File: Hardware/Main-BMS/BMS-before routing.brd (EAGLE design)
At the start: 153.4 x 107.6 mm, 121 parts, among them IC2 TLC6C5912-Q1, J1 SL03THROUGH_HOLE, J2 SL03THROUGH_HOLE, Q1 2N7002PW, Q10 2N7002PW, Q11 2N7002PW, Q12 2N7002PW, Q13 2N7002PW, Q14 2N7002PW, Q15 2N7002PW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

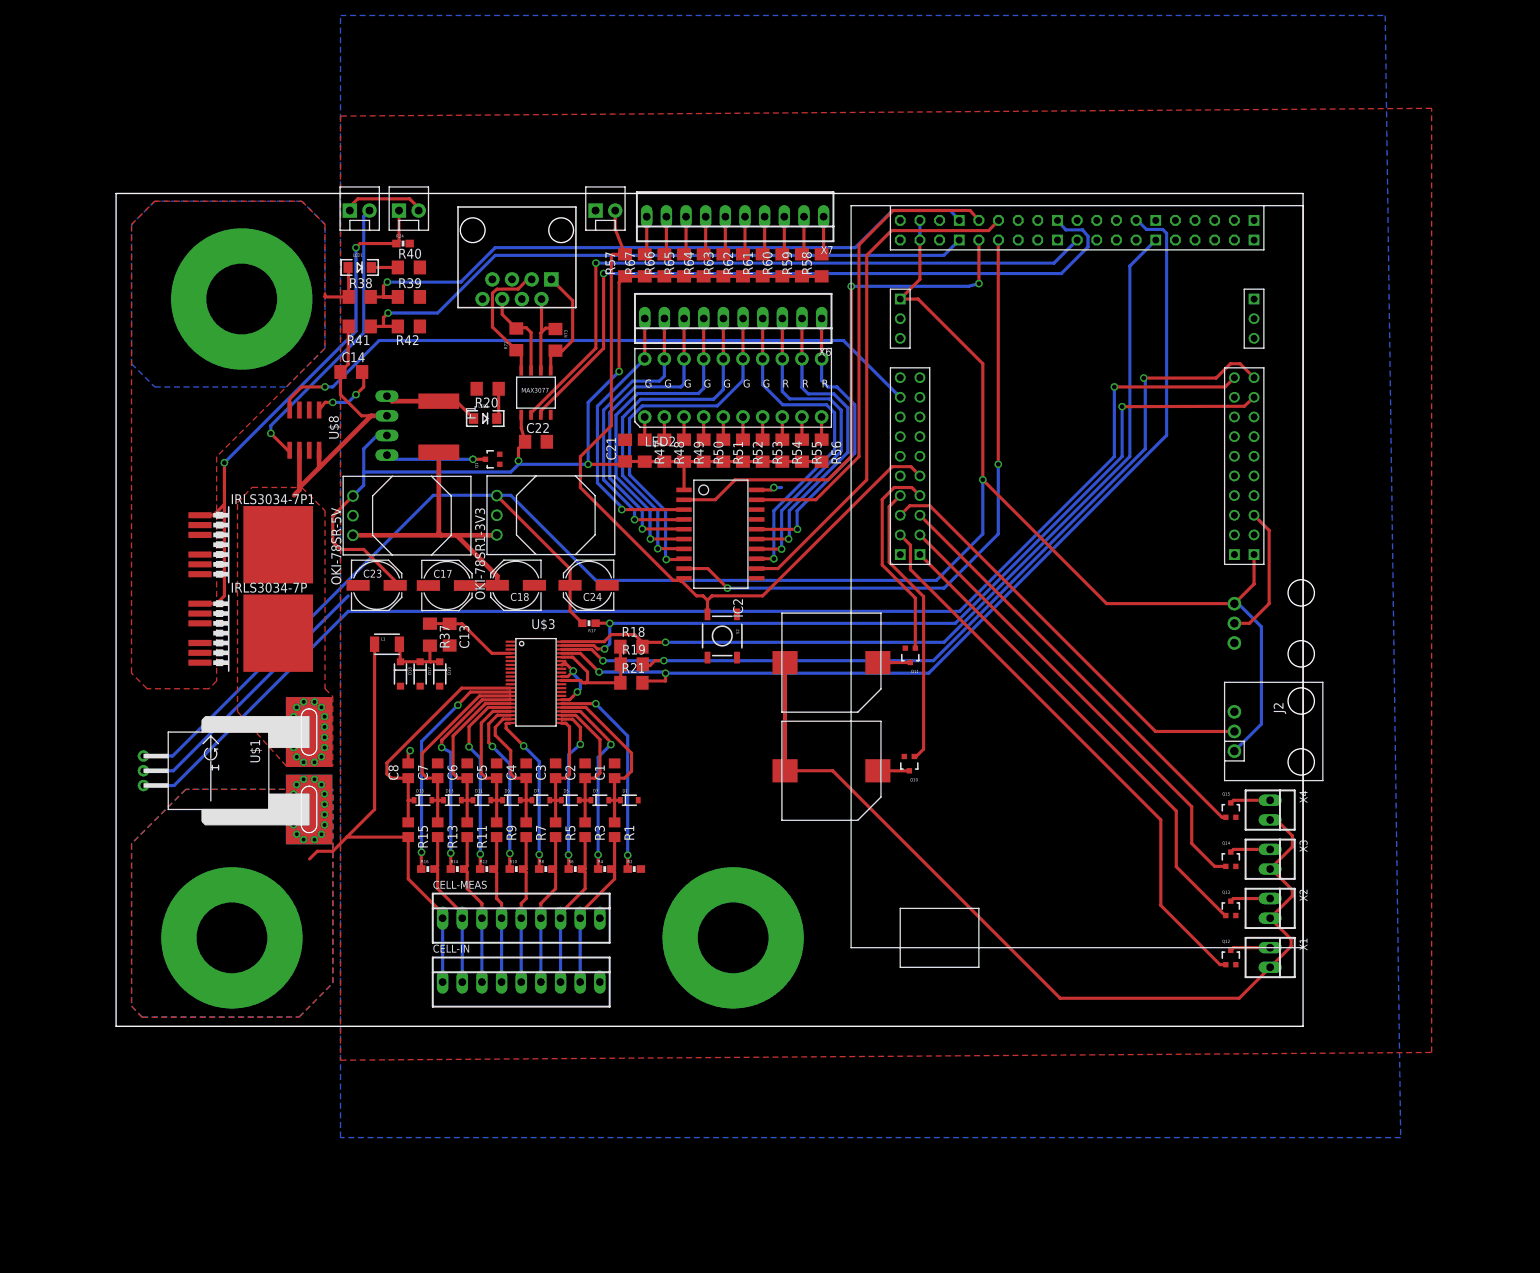
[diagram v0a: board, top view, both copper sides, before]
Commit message: PCB progress
First attempt at PCB design for BMS is mostly done
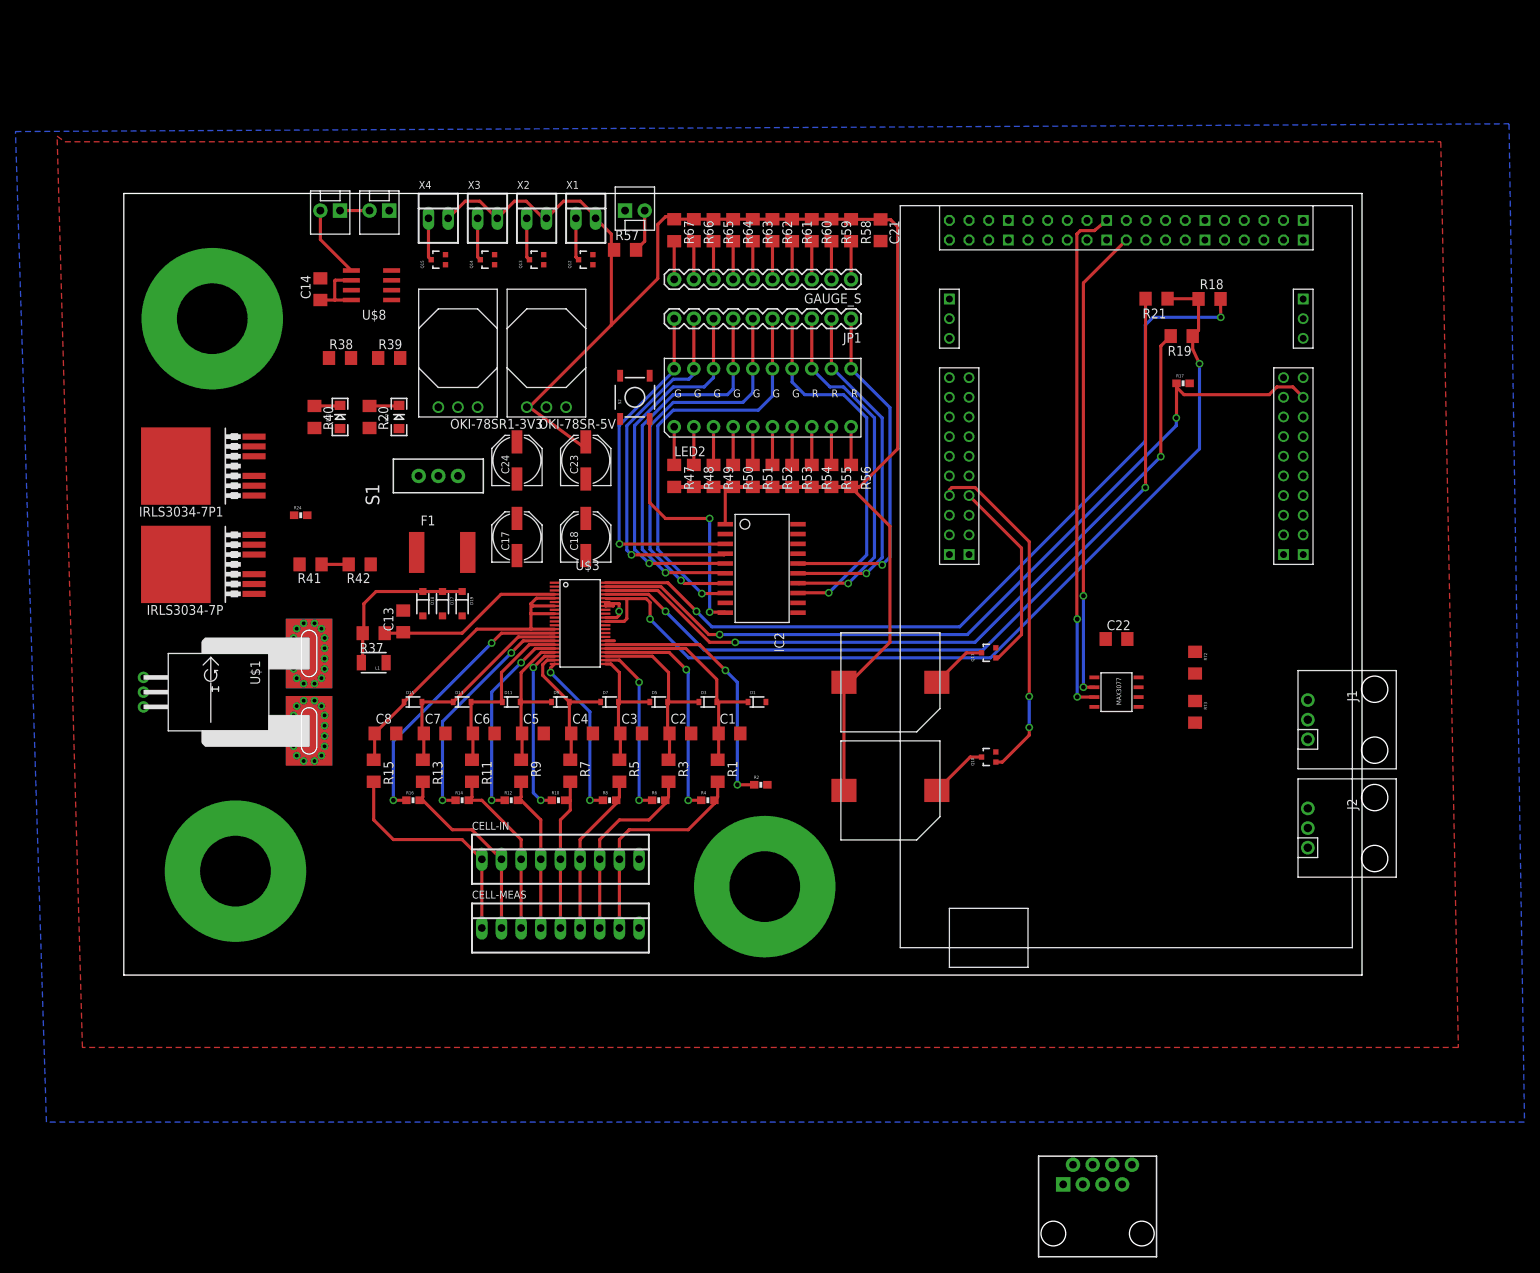
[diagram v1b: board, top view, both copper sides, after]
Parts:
- removed Q1: 2N7002PW, SparkFun-DiscreteSemi:SOT323
- removed X5: 22-23-2041, con-molex:22-23-2041
- removed X6, X7: 22-23-2101, con-molex:22-23-2101
- added GAUGE_S, JP1: M10", SparkFun-Connectors:1X10
- added S1: (no value), SparkFun-Electromechanical:SWITCH-SPDT
- C1, C2, C3, C4, C5, C6, C7, C8: device rcl:C0805 -> rcl:C1206
- R1, R11, R13, R15, R3, R5, R7, R9: device rcl:R0805 -> rcl:R1206
- moved U$14 149.8 mm to (125.8, -34.4), turned to 0 degrees
- moved X4 131.9 mm to (40.6, 96.8), turned to 0 degrees
- moved X3 130.7 mm to (47.0, 96.8), turned to 0 degrees
- moved X1 130.2 mm to (59.7, 96.8), turned to 0 degrees
- moved X2 130.1 mm to (53.3, 96.8), turned to 0 degrees
- moved Q15 124.7 mm to (40.6, 91.4), turned to 90 degrees
- moved Q14 123.4 mm to (47.0, 91.4), turned to 90 degrees
- moved Q12 122.8 mm to (59.7, 91.4), turned to 90 degrees
- moved Q13 122.8 mm to (53.3, 91.4), turned to 90 degrees
- moved R72 97.2 mm to (138.4, 39.4), turned to 270 degrees
- moved R73 95.6 mm to (138.4, 33.0)
- moved R18 87.2 mm to (140.3, 86.4)
- moved U$15 84.4 mm to (128.3, 35.6), turned to 270 degrees
- moved R21 84.1 mm to (133.4, 86.4), turned to 180 degrees
- moved R17 82.8 mm to (136.9, 75.5), turned to 0 degrees
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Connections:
- removed net LOGIC_SWITCH: Q1.1, U$13.3.3
- removed net N$5: Q1.3, X5.1
- new net CHARGER_CTL_B: U$13.7.6
- new net CHARGER_CTL_T: U$13.8.0
- new net CHARGER_I_MEAS: U$13.5.2
- new net V_CHECK_CHARGER_IN: U$13.5.1
- net 5V: no longer X5.2
- net FAN_CTL_1: now also U$13.2.4; no longer U$13.2.5
- net FAN_CTL_2: now also U$13.2.5; no longer U$13.2.7
- net FAN_CTL_4: now also U$13.2.7; no longer U$13.2.4
- net GAUGE_D: now also JP1.7; no longer X6.7
- net GND: now also S1.3; no longer Q1.2
- net N$2: now also S1.2; no longer X5.4
- net N$32: now also JP1.10; no longer X6.10
- net N$41: now also S1.1; no longer X5.3
- net N$43: now also JP1.9; no longer X6.9
- net N$44: now also JP1.8; no longer X6.8
- net N$46: now also JP1.6; no longer X6.6
- net N$47: now also JP1.5; no longer X6.5
- net N$48: now also JP1.4; no longer X6.4
- net N$49: now also JP1.3; no longer X6.3
- net N$50: now also JP1.2; no longer X6.2
- net N$51: now also JP1.1; no longer X6.1
- net N$75: now also GAUGE_S.1; no longer X7.1
- net N$76: now also GAUGE_S.2; no longer X7.2
- net N$77: now also GAUGE_S.3; no longer X7.3
- net N$78: now also GAUGE_S.4; no longer X7.4
- net N$79: now also GAUGE_S.5; no longer X7.5
- net N$80: now also GAUGE_S.6; no longer X7.6
- net N$81: now also GAUGE_S.7; no longer X7.7
- net N$82: now also GAUGE_S.8; no longer X7.8
- net N$83: now also GAUGE_S.9; no longer X7.9
- net N$84: now also GAUGE_S.10; no longer X7.10
- net PACK_GATE: now also U$13.6.0; no longer U$13.5.2
- net V_CHECK_ARRAY: now also U$13.5.3; no longer U$13.10.4
- net V_CHECK_OUT: now also U$13.5.4; no longer U$13.10.5
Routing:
- net +3V3: track 267.2 -> 0.00 mm, vias 1 -> 0
- net PACK_I_MEAS: track 168.1 -> 0.00 mm, vias 1 -> 0
- net BMS_VREG: track 18.1 -> 121.7 mm, vias 0 -> 2
- net PACK_GATE: track 86.5 -> 0.00 mm, vias 1 -> 0
- net V_CHECK_OUT: track 85.8 -> 0.00 mm, vias 1 -> 0
- net LED_CLR: track 82.5 -> 0.00 mm, vias 2 -> 0
- net V_CHECK_ARRAY: track 85.0 -> 3.51 mm, vias 1 -> 0
- net FAN_CTL_1: track 73.4 -> 0.00 mm
- net N$34: track 69.2 -> 0.00 mm, vias 2 -> 0
- net LED_SER_IN: track 68.1 -> 0.00 mm, vias 2 -> 0
- net LED_RCK: track 66.9 -> 0.00 mm
- net FAN_CTL_2: track 63.1 -> 0.00 mm
- net LED_SRCK: track 60.8 -> 0.00 mm
- net GAUGE_ON: track 99.3 -> 39.1 mm, vias 0 -> 2
- net FAN_CTL_3: track 60.1 -> 0.00 mm
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- removed copper zone on layer 1, net CELL_8
- removed copper zone on layer 16, net CELL_8
- removed copper zone on layer 1, net N$3
- removed copper zone on layer 16, net N$3
- removed copper zone on layer 1, net N$41
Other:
- board size 153.4 x 107.6 mm -> 160 x 101 mm
